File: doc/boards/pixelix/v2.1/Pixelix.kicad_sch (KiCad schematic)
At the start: 28 parts, among them J1 Conn_01x02, J2 Conn_01x02, J3 Conn_01x03, J4 Conn_01x02, J5 Conn_02x05_Odd_Even, J6 Conn_01x02, J7 Conn_01x03, J8 Conn_01x02, Q1 NMOS_GSD_BSS138, Q2 PMOS_GDS_STD26P3LLH6

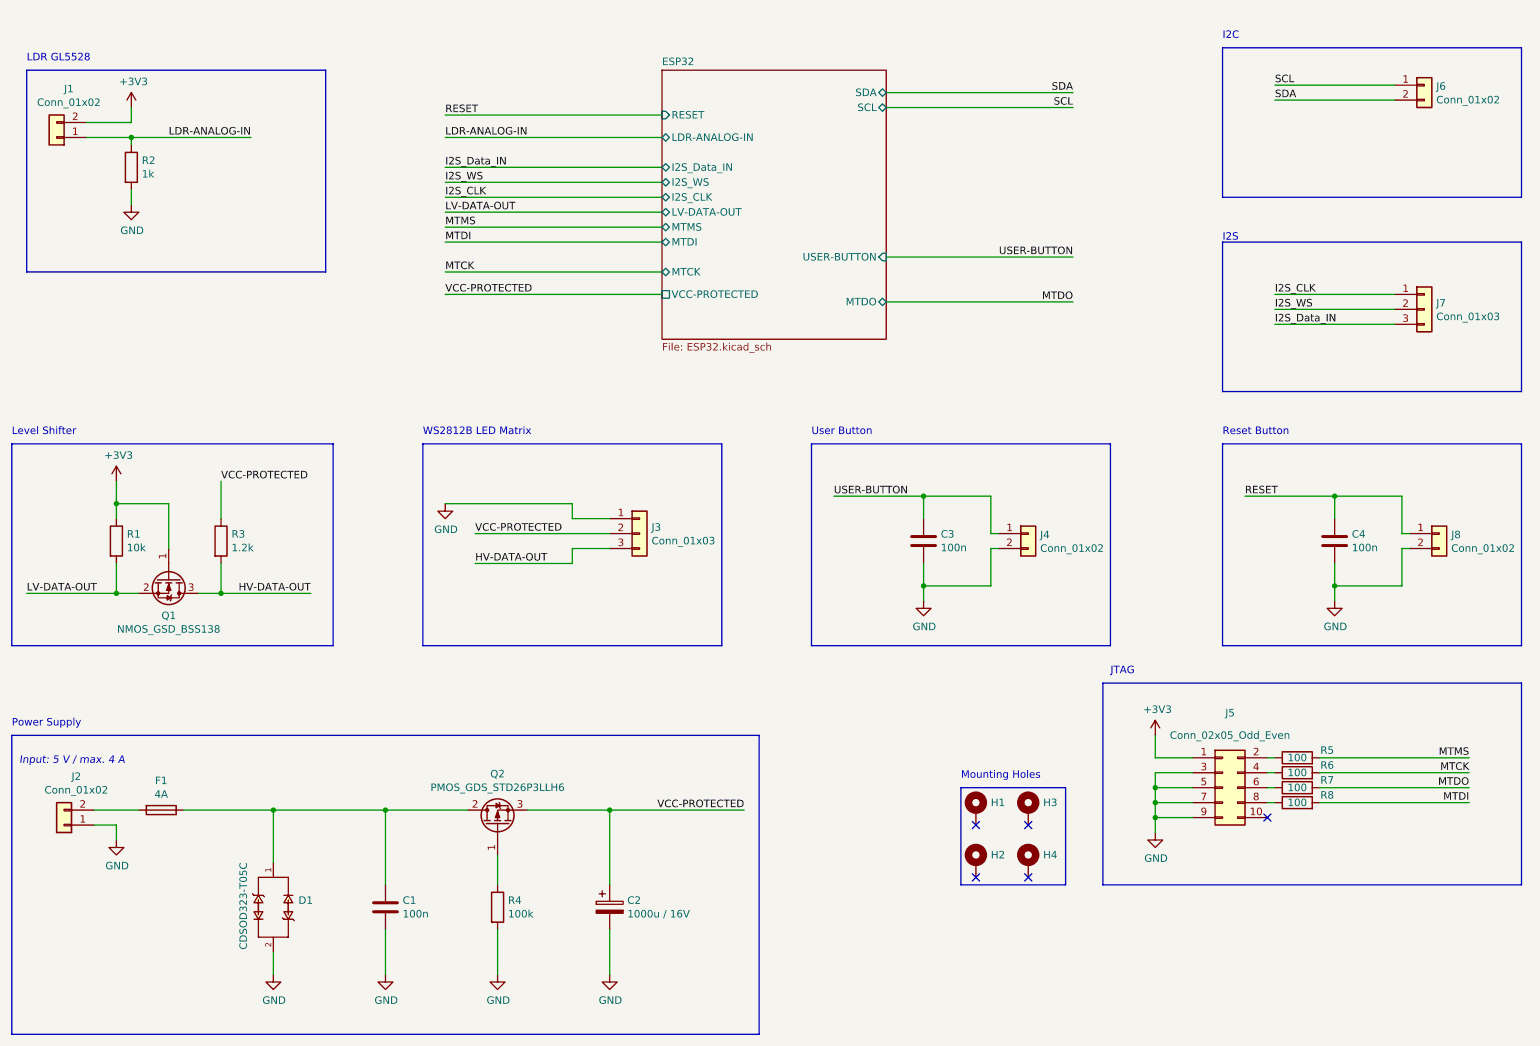
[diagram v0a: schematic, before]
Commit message: #91 HW v2.1: - One Wire added (see #40) - 3V3 and GND to I2S, I2C and One-Wire interface added - Testpoint added
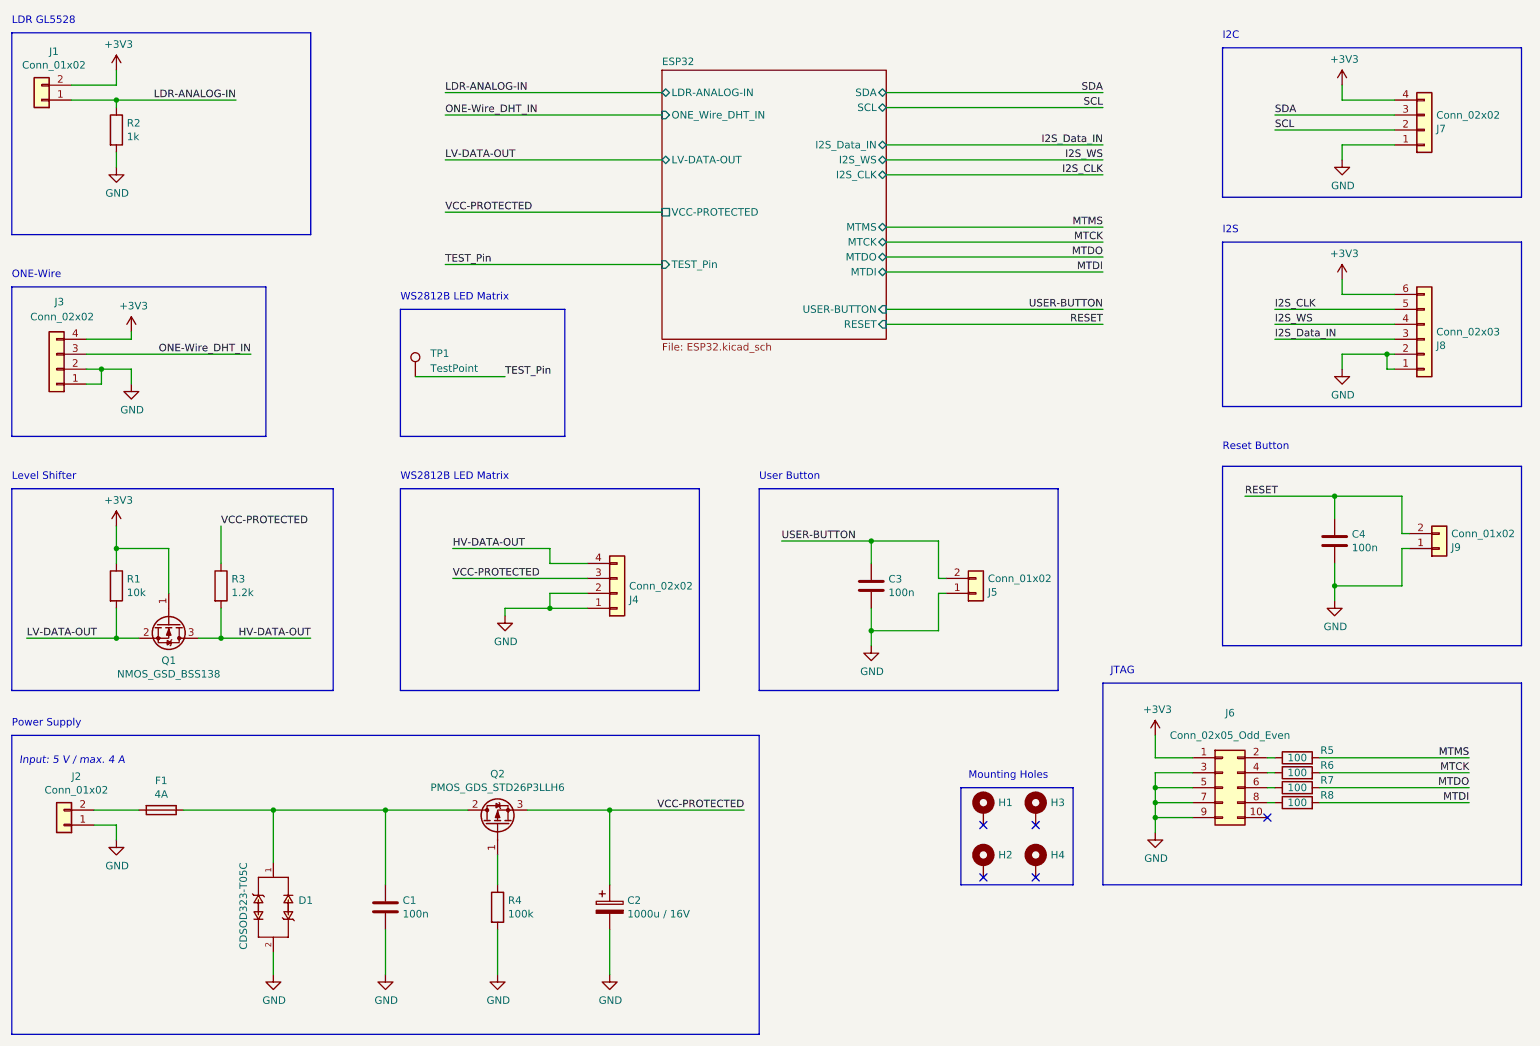
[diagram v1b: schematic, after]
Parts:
- added J3: Conn_02x02, footprints:66200421022, symbol Connector_Generic:Conn_01x04
- added TP1: TestPoint, Connector_PinHeader_2.54mm:PinHeader_1x01_P2.54mm_Vertical, symbol Connector:TestPoint
- J4: renamed from J3; value Conn_01x03 -> Conn_02x02; footprint footprints:66200311022 -> footprints:66200421022; symbol Connector_Generic:Conn_01x03 -> Connector_Generic:Conn_01x04; Part-No. 66200311022 -> 66200421022
- J7: renamed from J6; value Conn_01x02 -> Conn_02x02; footprint footprints:66200211022 -> footprints:66200421022; symbol Connector_Generic:Conn_01x02 -> Connector_Generic:Conn_01x04; Part-No. 66200211022 -> 66200421022
- J8: renamed from J7; value Conn_01x03 -> Conn_02x03; footprint footprints:66200311022 -> footprints:66200621022; symbol Connector_Generic:Conn_01x03 -> Connector_Generic:Conn_01x06; Part-No. 66200311022 -> 66200621022
- renumbered J4 to J5, J5 to J6, J8 to J9
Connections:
- net +3V3: now also J7.4 (Pin_4), J8.6 (Pin_6), J3.4 (Pin_4)
- net GND: now also J4.2 (Pin_2), J5.1 (Pin_1), J7.1 (Pin_1), J8.1 (Pin_1), J8.2 (Pin_2), J9.1 (Pin_1), J3.1 (Pin_1), J3.2 (Pin_2); no longer J5.2 (Pin_2), J9.2 (Pin_2)
- net HV-DATA-OUT: now also J4.4 (Pin_4); no longer J4.3 (Pin_3)
- net I2S_CLK: now also J8.5 (Pin_5); no longer J8.1 (Pin_1)
- net I2S_WS: now also J8.4 (Pin_4); no longer J8.2 (Pin_2)
- net RESET: now also J9.2 (Pin_2); no longer J9.1 (Pin_1)
- net SCL: now also J7.2 (Pin_2); no longer J7.1 (Pin_1)
- net SDA: now also J7.3 (Pin_3); no longer J7.2 (Pin_2)
- net USER-BUTTON: now also J5.2 (Pin_2); no longer J5.1 (Pin_1)
- net VCC-PROTECTED: now also J4.3 (Pin_3); no longer J4.2 (Pin_2)
- new net ONE-Wire_DHT_IN: J3.3 (Pin_3)
- new net TEST_Pin: TP1.1
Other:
- sheet ESP32 ports: added ONE_Wire_DHT_IN, TEST_Pin; removed none
- note added: "ONE-Wire"
- moved on the sheet: C3, H1, H2, H3, H4, J1, J5, Q1, R1, R2, R3
